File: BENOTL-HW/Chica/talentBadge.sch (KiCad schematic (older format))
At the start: 63 parts, among them P1 USB_A, P2 OLED, P3 Batt, P4 PS, P5 sd_card_spi, Q1 MMBT3904, Q2 MMBT3904, Q3 IR phototransistor, SW1 B1, SW2 B2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

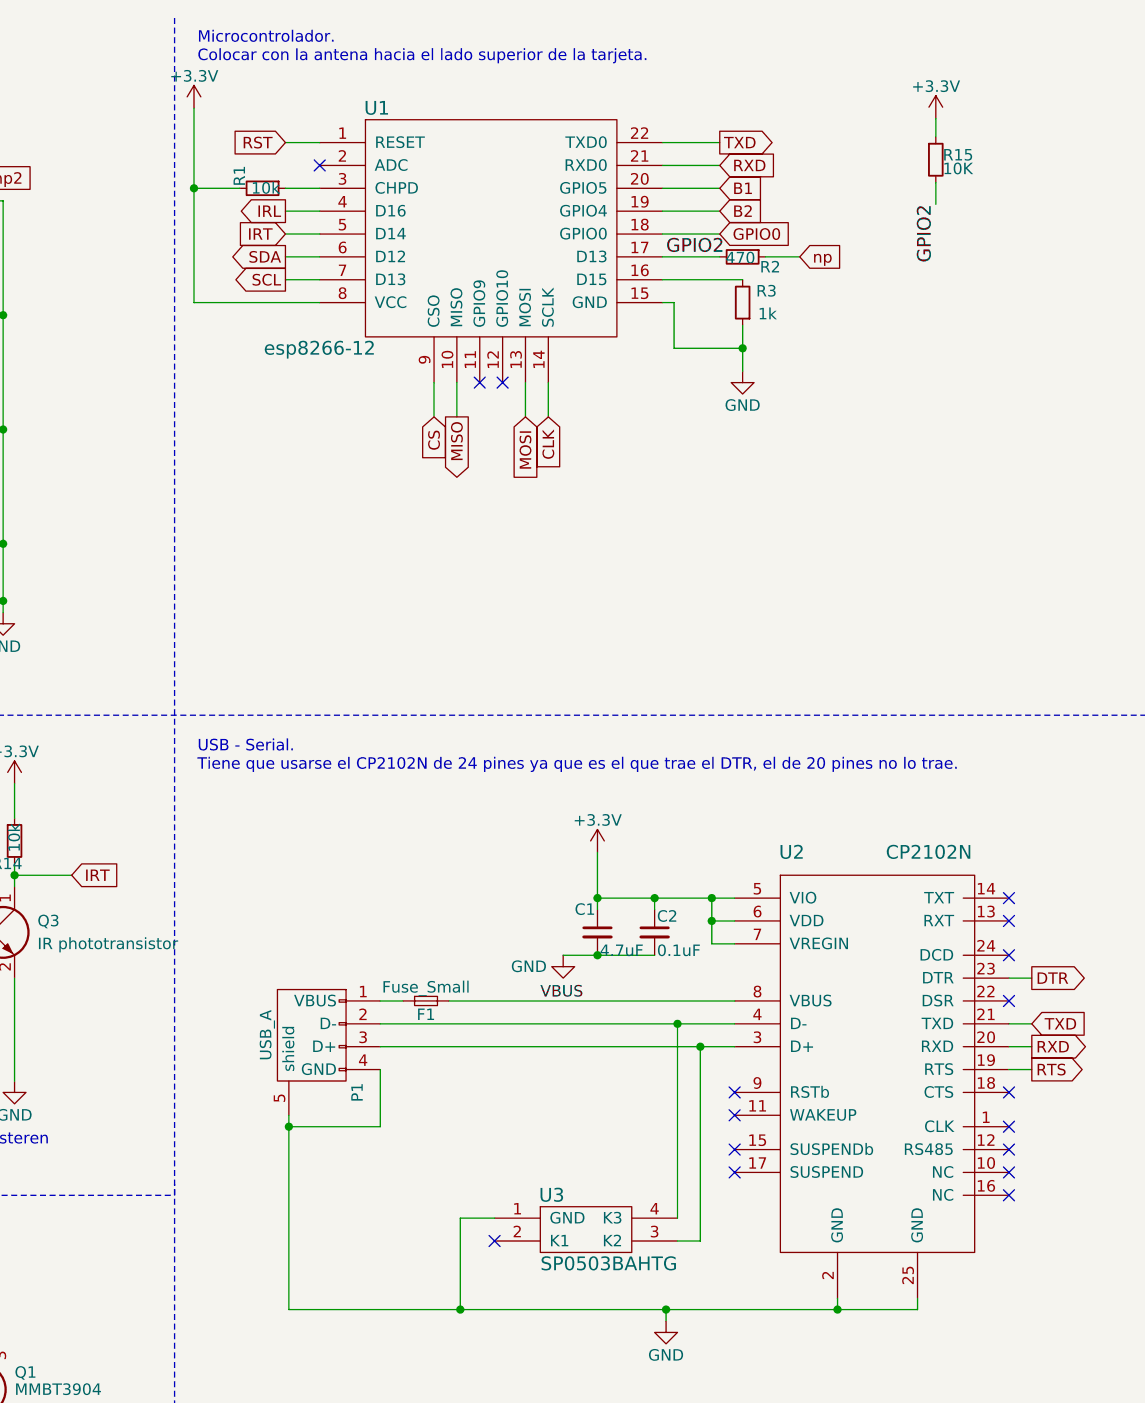
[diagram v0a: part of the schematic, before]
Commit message: Routeo y layout de chica - incompleto.
Tuve que cambiar el grid del schematico por que en la seccion del esp estabamovido.
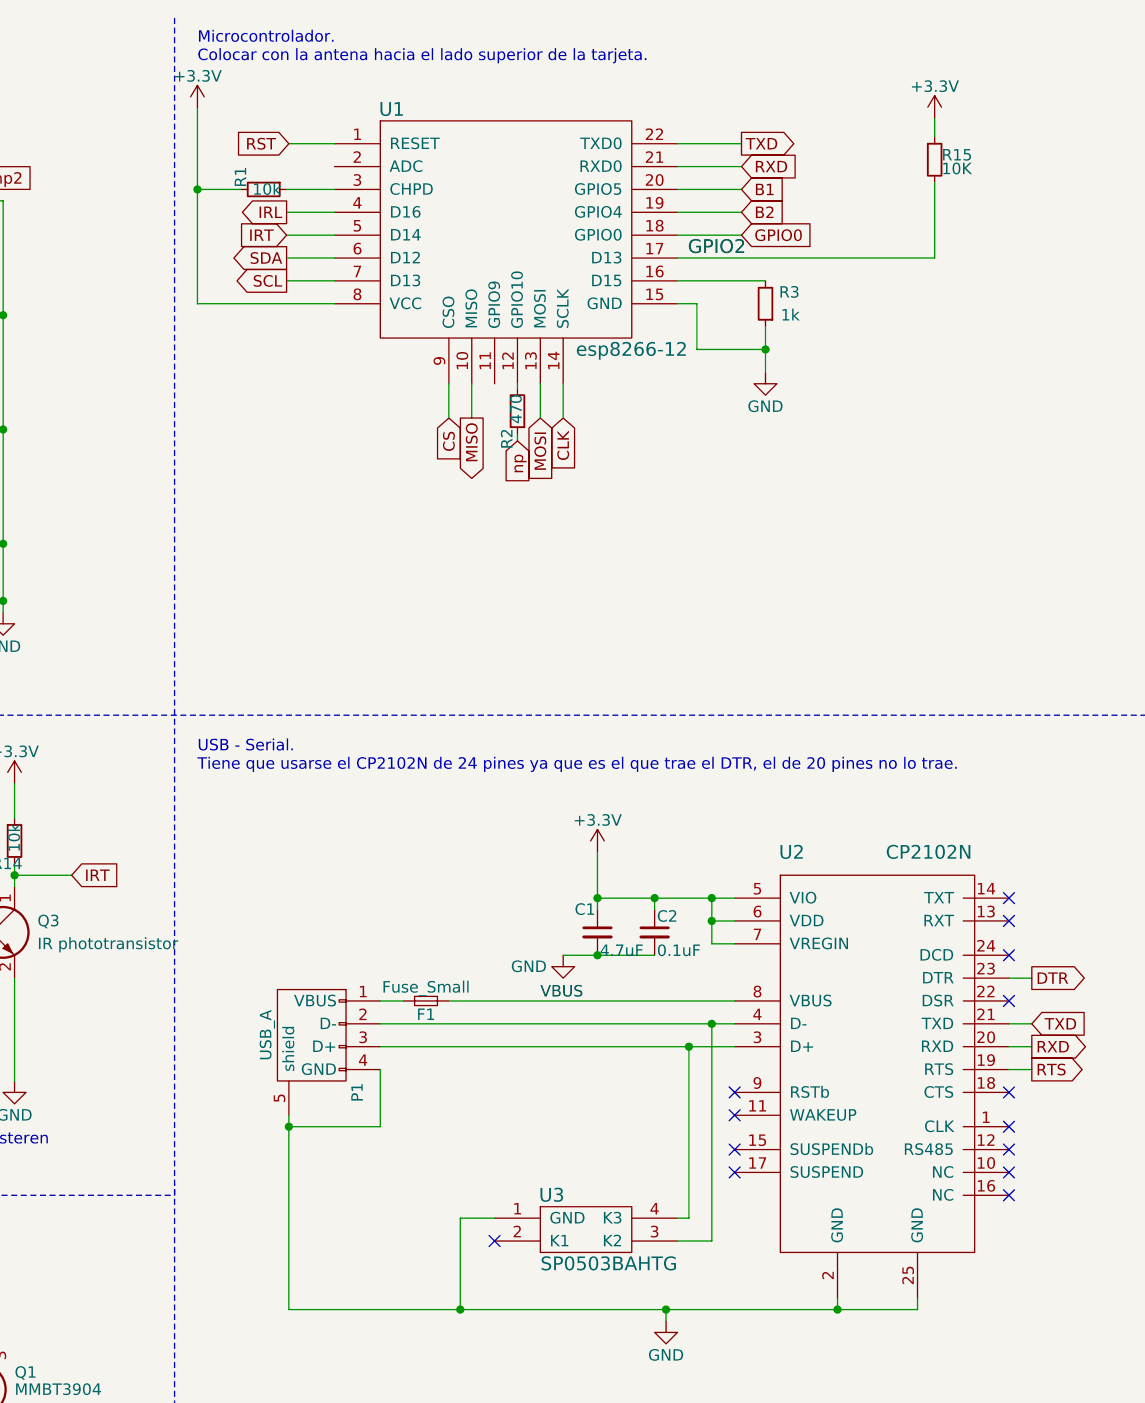
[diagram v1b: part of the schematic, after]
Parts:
- R15: footprint (none) -> Resistors_SMD:R_0805_HandSoldering
- U1: footprint talentBadge:ESP-12E_SMD -> (none)
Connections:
- net GPIO2: no longer R2.2
- net SCL: no longer U1.7 (D13)
- net at P1.3 (D+), U2.3 (D+): now also U3.4 (K3); no longer U3.3 (K2)
- net at P1.2 (D-), U2.4 (D-): now also U3.3 (K2); no longer U3.4 (K3)
- net at U1.12 (GPIO10): now also R2.2
- no-connect marks 22 -> 19
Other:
- moved on the sheet: R2, R3

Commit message: Routeo Chica completo
Se cambio pin vcc y gnd en conector oled de posicion ya que estaban al reves.
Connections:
- net +3V3: now also P2.2 (P2); no longer P2.1 (P1)
- net GND: now also P2.1 (P1); no longer P2.2 (P2)
- net GPIO2: now also R2.2
- net SCL: now also U1.7 (D13)
- net at U1.12 (GPIO10): no longer R2.2
- no-connect marks 19 -> 6
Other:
- moved on the sheet: R2
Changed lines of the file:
@@
 $EndComp
 $Comp
-L GND #PWR8
+L GND #PWR01
 U 1 1 5A821F87
 P 2900 7450
-F 0 "#PWR8" H 2900 7200 50  0001 C CNN
+F 0 "#PWR01" H 2900 7200 50  0001 C CNN
 F 1 "GND" H 2900 7300 50  0000 C CNN
 F 2 "" H 2900 7450 50  0000 C CNN
@@
 $EndComp
 $Comp
-L GND #PWR6
+L GND #PWR02
 U 1 1 5A8731F6
 P 2550 3100
-F 0 "#PWR6" H 2550 2850 50  0001 C CNN
+F 0 "#PWR02" H 2550 2850 50  0001 C CNN
 F 1 "GND" H 2550 2950 50  0000 C CNN
 F 2 "" H 2550 3100 50  0000 C CNN
@@
 np1
 $Comp
-L GND #PWR11
+L GND #PWR03
 U 1 1 5A87C4F2
 P 4350 3100
-F 0 "#PWR11" H 4350 2850 50  0001 C CNN
+F 0 "#PWR03" H 4350 2850 50  0001 C CNN
 F 1 "GND" H 4350 2950 50  0000 C CNN
 F 2 "" H 4350 3100 50  0000 C CNN
@@
 np2
 $Comp
-L GND #PWR16
+L GND #PWR04
 U 1 1 5A87E79A
 P 6150 3100
-F 0 "#PWR16" H 6150 2850 50  0001 C CNN
+F 0 "#PWR04" H 6150 2850 50  0001 C CNN
 F 1 "GND" H 6150 2950 50  0000 C CNN
 F 2 "" H 6150 3100 50  0000 C CNN
@@
 $EndComp
 $Comp
-L GND #PWR3
+L GND #PWR05
 U 1 1 5A884E23
 P 1700 6900
-F 0 "#PWR3" H 1700 6650 50  0001 C CNN
+F 0 "#PWR05" H 1700 6650 50  0001 C CNN
 F 1 "GND" H 1700 6750 50  0000 C CNN
 F 2 "" H 1700 6900 50  0000 C CNN
@@
 $EndComp
 $Comp
-L +3.3V #PWR5
+L +3.3V #PWR06
 U 1 1 5A8855B6
 P 2250 6200
-F 0 "#PWR5" H 2250 6050 50  0001 C CNN
+F 0 "#PWR06" H 2250 6050 50  0001 C CNN
 F 1 "+3.3V" H 2250 6340 50  0000 C CNN
 F 2 "" H 2250 6200 50  0000 C CNN
@@
 	1    0    0    -1
 $EndComp
-Text GLabel 8400 2350 3    50   Input ~ 0
+Text GLabel 10560 1550 2    50   Output ~ 0
 np
 Text GLabel 2550 1200 2    50   Input ~ 0
 np
 $Comp
-L +3.3V #PWR1
+L +3.3V #PWR07
 U 1 1 5A888CD9
 P 1000 950
-F 0 "#PWR1" H 1000 800 50  0001 C CNN
+F 0 "#PWR07" H 1000 800 50  0001 C CNN
 F 1 "+3.3V" H 1000 1090 50  0000 C CNN
 F 2 "" H 1000 950 50  0000 C CNN
@@
 $EndComp
 $Comp
-L +3.3V #PWR7
+L +3.3V #PWR08
 U 1 1 5A888D9D
 P 2850 950
-F 0 "#PWR7" H 2850 800 50  0001 C CNN
+F 0 "#PWR08" H 2850 800 50  0001 C CNN
 F 1 "+3.3V" H 2850 1090 50  0000 C CNN
 F 2 "" H 2850 950 50  0000 C CNN
@@
 $EndComp
 $Comp
-L +3.3V #PWR12
+L +3.3V #PWR09
 U 1 1 5A88959B
 P 4550 950
-F 0 "#PWR12" H 4550 800 50  0001 C CNN
+F 0 "#PWR09" H 4550 800 50  0001 C CNN
 F 1 "+3.3V" H 4550 1090 50  0000 C CNN
 F 2 "" H 4550 950 50  0000 C CNN
@@
 $EndComp
 $Comp
-L +3.3V #PWR19
+L +3.3V #PWR010
 U 1 1 5A889CBB
 P 7000 895
-F 0 "#PWR19" H 7000 745 50  0001 C CNN
+F 0 "#PWR010" H 7000 745 50  0001 C CNN
 F 1 "+3.3V" H 7000 1035 50  0000 C CNN
 F 2 "" H 7000 895 50  0000 C CNN
@@
 $EndComp
 $Comp
-L GND #PWR23
+L GND #PWR011
 U 1 1 5A889D35
 P 9485 2050
-F 0 "#PWR23" H 9485 1800 50  0001 C CNN
+F 0 "#PWR011" H 9485 1800 50  0001 C CNN
 F 1 "GND" H 9485 1900 50  0000 C CNN
 F 2 "" H 9485 2050 50  0000 C CNN
@@
 L R_Small R2
 U 1 1 5A88A940
-P 8400 2220
-F 0 "R2" V 8445 2295 50  0000 L CNN
-F 1 "470" V 8405 2145 50  0000 L CNN
-F 2 "Resistors_SMD:R_0805_HandSoldering" H 8400 2220 50  0001 C CNN
-F 3 "" H 8400 2220 50  0000 C CNN
-	1    8400 2220
-	-1   0    0    1
+P 10360 1550
+F 0 "R2" V 10405 1625 50  0000 L CNN
+F 1 "470" V 10365 1475 50  0000 L CNN
+F 2 "Resistors_SMD:R_0805_HandSoldering" H 10360 1550 50  0001 C CNN
+F 3 "" H 10360 1550 50  0000 C CNN
+	1    10360 1550
+	0    1    1    0
 $EndComp
 Text GLabel 10650 4900 2    50   Input ~ 0
@@
 MISO
 $Comp
-L GND #PWR2
+L GND #PWR012
 U 1 1 5A89D556
 P 1400 4300
-F 0 "#PWR2" H 1400 4050 50  0001 C CNN
+F 0 "#PWR012" H 1400 4050 50  0001 C CNN
 F 1 "GND" H 1400 4150 50  0000 C CNN
 F 2 "" H 1400 4300 50  0000 C CNN
@@
 $EndComp
 $Comp
-L +3.3V #PWR4
+L +3.3V #PWR013
 U 1 1 5A89DD80
 P 1900 3850
-F 0 "#PWR4" H 1900 3700 50  0001 C CNN
+F 0 "#PWR013" H 1900 3700 50  0001 C CNN
 F 1 "+3.3V" H 1900 3990 50  0000 C CNN
 F 2 "" H 1900 3850 50  0000 C CNN
@@
 $EndComp
 $Comp
-L GND #PWR9
+L GND #PWR014
 U 1 1 5A8A120C
 P 3050 5200
-F 0 "#PWR9" H 3050 4950 50  0001 C CNN
+F 0 "#PWR014" H 3050 4950 50  0001 C CNN
 F 1 "GND" H 3050 5050 50  0000 C CNN
 F 2 "" H 3050 5200 50  0000 C CNN
@@
 MISO
 $Comp
-L +3.3V #PWR21
+L +3.3V #PWR015
 U 1 1 5A8ACE92
 P 8750 4150
-F 0 "#PWR21" H 8750 4000 50  0001 C CNN
+F 0 "#PWR015" H 8750 4000 50  0001 C CNN
 F 1 "+3.3V" H 8750 4290 50  0000 C CNN
 F 2 "" H 8750 4150 50  0000 C CNN
@@
 $EndComp
 $Comp
-L GND #PWR20
+L GND #PWR016
 U 1 1 5A8B6B0C
 P 8600 4600
-F 0 "#PWR20" H 8600 4350 50  0001 C CNN
+F 0 "#PWR016" H 8600 4350 50  0001 C CNN
 F 1 "GND" H 8450 4550 50  0000 C CNN
 F 2 "" H 8600 4600 50  0000 C CNN
@@
 $EndComp
 $Comp
-L CP2102N U2
-U 1 1 5A8B808C
-P 9950 5900
-F 0 "U2" H 9600 7650 60  0000 C CNN
-F 1 "CP2102N" H 10200 7650 60  0000 C CNN
-F 2 "talentBadge:QFN-24-5x5mm_Pitch0.50mm" H 9850 6300 60  0001 C CNN
-F 3 "https://www.mouser.com/ds/2/368/cp2102n-datasheet-1082647.pdf" H 9850 6300 60  0001 C CNN
-F 4 "CP2102N-A01-GQFN24" H 9950 5900 60  0001 C CNN "PartNo"
-	1    9950 5900
-	1    0    0    -1
-$EndComp
-$Comp
-L GND #PWR22
+L GND #PWR017
 U 1 1 5A8BA4F2
 P 9050 6200
-F 0 "#PWR22" H 9050 5950 50  0001 C CNN
+F 0 "#PWR017" H 9050 5950 50  0001 C CNN
 F 1 "GND" H 9050 6050 50  0000 C CNN
 F 2 "" H 9050 6200 50  0000 C CNN
@@
 $EndComp
 $Comp
-L +3.3V #PWR10
+L +3.3V #PWR018
 U 1 1 5A8CF103
 P 3700 6000
-F 0 "#PWR10" H 3700 5850 50  0001 C CNN
+F 0 "#PWR018" H 3700 5850 50  0001 C CNN
 F 1 "+3.3V" H 3700 6140 50  0000 C CNN
 F 2 "" H 3700 6000 50  0000 C CNN
@@
 $EndComp
 $Comp
-L +3.3V #PWR13
+L +3.3V #PWR019
 U 1 1 5A8CF265
-P 4650 4300
-F 0 "#PWR13" H 4650 4150 50  0001 C CNN
-F 1 "+3.3V" H 4650 4440 50  0000 C CNN
-F 2 "" H 4650 4300 50  0000 C CNN
-F 3 "" H 4650 4300 50  0000 C CNN
-	1    4650 4300
-	1    0    0    -1
-$EndComp
-$Comp
-L GND #PWR14
+P 4535 4300
+F 0 "#PWR019" H 4535 4150 50  0001 C CNN
+F 1 "+3.3V" H 4535 4440 50  0000 C CNN
+F 2 "" H 4535 4300 50  0000 C CNN
+F 3 "" H 4535 4300 50  0000 C CNN
+	1    4535 4300
+	1    0    0    -1
+$EndComp
+$Comp
+L GND #PWR020
 U 1 1 5A8CFC33
 P 4650 4900
-F 0 "#PWR14" H 4650 4650 50  0001 C CNN
+F 0 "#PWR020" H 4650 4650 50  0001 C CNN
 F 1 "GND" H 4650 4750 50  0000 C CNN
 F 2 "" H 4650 4900 50  0000 C CNN
@@
 Text GLabel 4550 4650 0    50   Input ~ 0
 SCL
-NoConn ~ 10550 5550
-NoConn ~ 10550 5650
-NoConn ~ 10550 5450
-NoConn ~ 10550 5350
 Text GLabel 7390 1650 0    50   Output ~ 0
 SCL
@@
 	7000 895  7000 1750
 Wire Wire Line
-	10225 1550 9100 1550
+	9100 1550 10260 1550
 Wire Wire Line
 	10550 4900 10650 4900
@@
 Connection ~ 3900 6850
 Wire Wire Line
-	4650 4300 4650 4450
-Wire Wire Line
-	4650 4450 4800 4450
-Wire Wire Line
-	4800 4550 4650 4550
-Wire Wire Line
-	4650 4550 4650 4900
+	4535 4300 4535 4550
+Wire Wire Line
+	4650 4450 4650 4900
 Wire Wire Line
 	4550 4650 4800 4650
@@
 	5650 4100 5700 4100
 $Comp
-L GND #PWR15
+L GND #PWR021
 U 1 1 5A9146B5
 P 5700 5150
-F 0 "#PWR15" H 5700 4900 50  0001 C CNN
+F 0 "#PWR021" H 5700 4900 50  0001 C CNN
 F 1 "GND" H 5700 5000 50  0000 C CNN
 F 2 "" H 5700 5150 50  0000 C CNN
@@
 $EndComp
 $Comp
-L GND #PWR18
+L GND #PWR022
 U 1 1 5A914774
 P 6200 5150
-F 0 "#PWR18" H 6200 4900 50  0001 C CNN
+F 0 "#PWR022" H 6200 4900 50  0001 C CNN
 F 1 "GND" H 6200 5000 50  0000 C CNN
 F 2 "" H 6200 5150 50  0000 C CNN
@@
 	6200 4700 6200 5150
 $Comp
-L +3.3V #PWR17
+L +3.3V #PWR023
 U 1 1 5A916FB2
 P 6200 3850
-F 0 "#PWR17" H 6200 3700 50  0001 C CNN
+F 0 "#PWR023" H 6200 3700 50  0001 C CNN
 F 1 "+3.3V" H 6200 3990 50  0000 C CNN
 F 2 "" H 6200 3850 50  0000 C CNN
@@
 $EndComp
 $Comp
-L +3.3V #PWR24
+L +3.3V #PWR024
 U 1 1 5A8CED38
 P 10225 940
-F 0 "#PWR24" H 10225 790 50  0001 C CNN
+F 0 "#PWR024" H 10225 790 50  0001 C CNN
 F 1 "+3.3V" H 10225 1080 50  0000 C CNN
 F 2 "" H 10225 940 50  0000 C CNN
@@
 Text Label 9145 1550 0    60   ~ 0
 GPIO2
-NoConn ~ 9350 5200
-NoConn ~ 10550 4350
-NoConn ~ 10550 4450
-NoConn ~ 10550 4600
-NoConn ~ 10550 5200
-NoConn ~ 9350 5300
-NoConn ~ 9350 5450
-NoConn ~ 9350 5550
-NoConn ~ 10550 4800
 NoConn ~ 3250 5100
 NoConn ~ 3250 4400
@@
 	7400 1050 7600 1050
 Wire Wire Line
-	8400 2100 8400 2120
-Wire Wire Line
-	8400 2320 8400 2350
-Wire Wire Line
 	8500 2100 8500 2250
 Wire Wire Line
@@
 Wire Wire Line
 	7390 1550 7600 1550
-Wire Wire Line
-	7605 1650 7390 1650
 Wire Wire Line
 	7000 1750 7600 1750
@@
 	7190 1250 7000 1250
 Connection ~ 7000 1250
+Wire Wire Line
+	7390 1650 7600 1650
+Wire Wire Line
+	4650 4450 4800 4450
+Wire Wire Line
+	4535 4550 4800 4550
+$Comp
+L CP2102N U2
+U 1 1 5A8B808C
+P 9950 5900
+F 0 "U2" H 9600 7650 60  0000 C CNN
+F 1 "CP2102N" H 10200 7650 60  0000 C CNN
+F 2 "talentBadge:QFN-24-5x5mm_Pitch0.50mm" H 9850 6300 60  0001 C CNN
+F 3 "https://www.mouser.com/ds/2/368/cp2102n-datasheet-1082647.pdf" H 9850 6300 60  0001 C CNN
+F 4 "CP2102N-A01-GQFN24" H 9950 5900 60  0001 C CNN "PartNo"
+	1    9950 5900
+	1    0    0    -1
+$EndComp
+Connection ~ 10225 1550
+Wire Wire Line
+	10460 1550 10560 1550
 $EndSCHEMATC

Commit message: Add no conection
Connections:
- no-connect marks 6 -> 22
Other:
- note removed: "TBadge"

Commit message: R3 y R2 agregado al BOM
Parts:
- R2: PartNo (none) -> CR0805-FX-4700ELF
- R3: PartNo (none) -> RC0805JR-071KL
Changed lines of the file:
@@
 Sheet 1 1
 Title "The badge of the Lands"
-Date "2018-12-31"
-Rev "0.2"
+Date "2018-03-07"
+Rev "0.3"
 Comp "Unofficial Badge of Talent Land 2018"
 Comment1 "Andres Sabas"
-Comment2 ""
-Comment3 ""
-Comment4 ""
+Comment2 "Eden Candelas"
+Comment3 "Eduardo Contreras"
+Comment4 "Gustavo Reynaga"
 $EndDescr
 $Comp
@@
 F 2 "Resistors_SMD:R_0805_HandSoldering" H 10360 1550 50  0001 C CNN
 F 3 "" H 10360 1550 50  0000 C CNN
+F 4 "CR0805-FX-4700ELF" V 10360 1550 60  0001 C CNN "PartNo"
 	1    10360 1550
 	0    1    1    0
@@
 F 2 "Resistors_SMD:R_0805_HandSoldering" H 9485 1750 50  0001 C CNN
 F 3 "" H 9485 1750 50  0000 C CNN
+F 4 "RC0805JR-071KL" H 9485 1750 60  0001 C CNN "PartNo"
 	1    9485 1750
 	-1   0    0    1

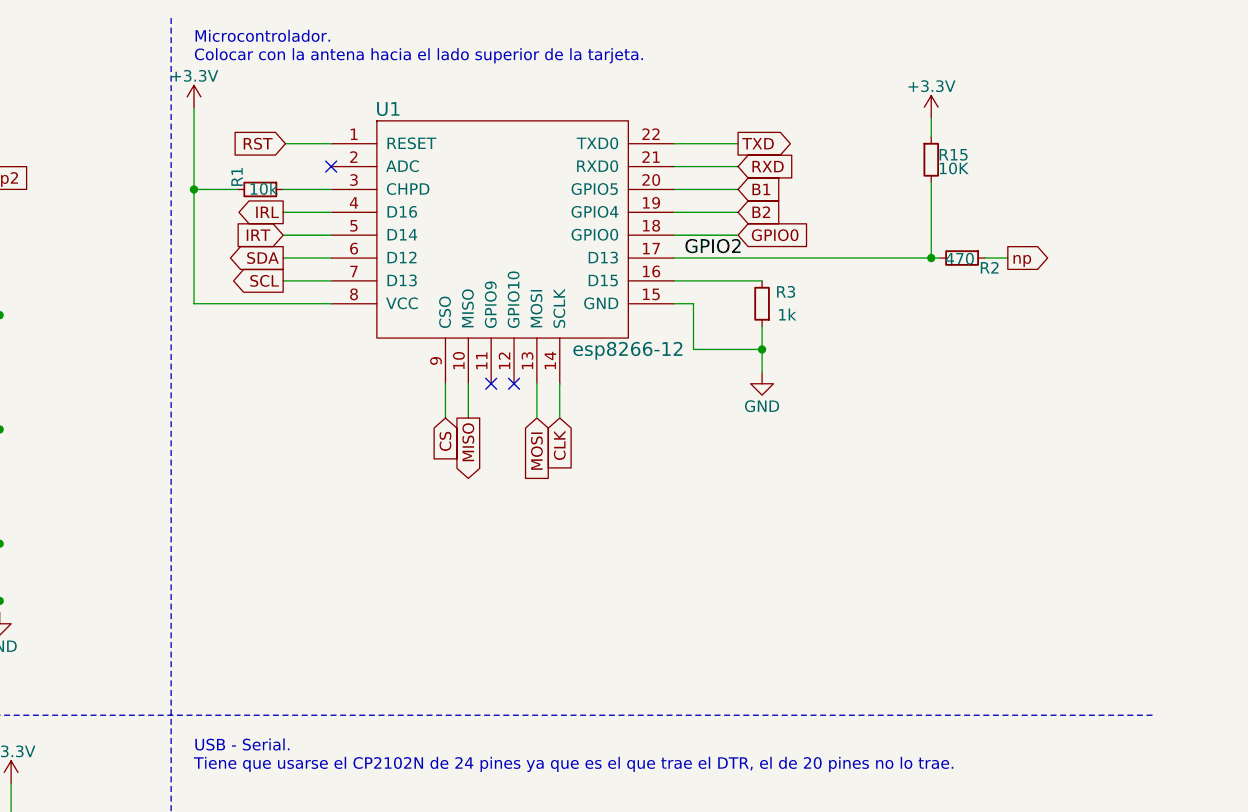
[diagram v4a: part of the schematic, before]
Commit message: Cambiado ESP8266 a ESP-WROOM-02
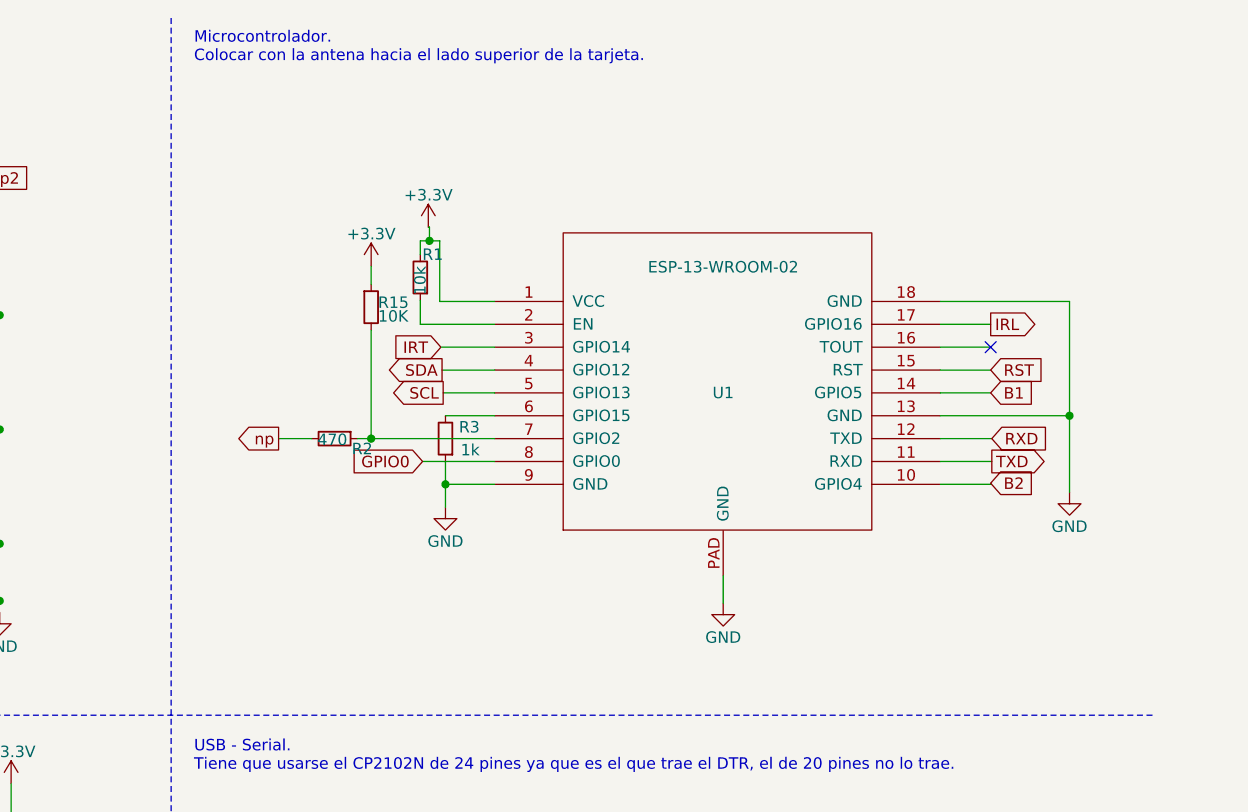
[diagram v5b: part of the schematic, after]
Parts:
- removed U1: esp8266-12, symbol esp8266-12
- added U1: ESP-13-WROOM-02, symbol ESP-13-WROOM-02
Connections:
- net +3V3: now also U1.1 (VCC)
- net B1: now also U1.14 (GPIO5)
- net B2: now also U1.10 (GPIO4)
- net GND: now also U1.13 (GND), U1.18 (GND), U1.9 (GND), U1.PAD (GND)
- net GPIO0: now also U1.8 (GPIO0)
- net IRL: now also U1.17 (GPIO16)
- net IRT: now also U1.3 (GPIO14)
- net RST: now also U1.15 (RST)
- net RXD: now also U1.12 (TXD)
- net SCL: now also U1.5 (GPIO13)
- net SDA: now also U1.4 (GPIO12)
- net TXD: now also U1.11 (RXD)
- net np: now also R2.2; no longer R2.1
- net at R3.2: now also U1.6 (GPIO15)
- net at R1.1: now also U1.2 (EN)
- net GPIO2: no longer names the net of R15.2
- net GPIO2: now also R2.1, U1.7 (GPIO2); no longer R2.2
- no-connect marks 22 -> 20
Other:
- moved on the sheet: R1, R15, R2, R3
